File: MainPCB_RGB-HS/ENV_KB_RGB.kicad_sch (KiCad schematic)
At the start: 405 parts

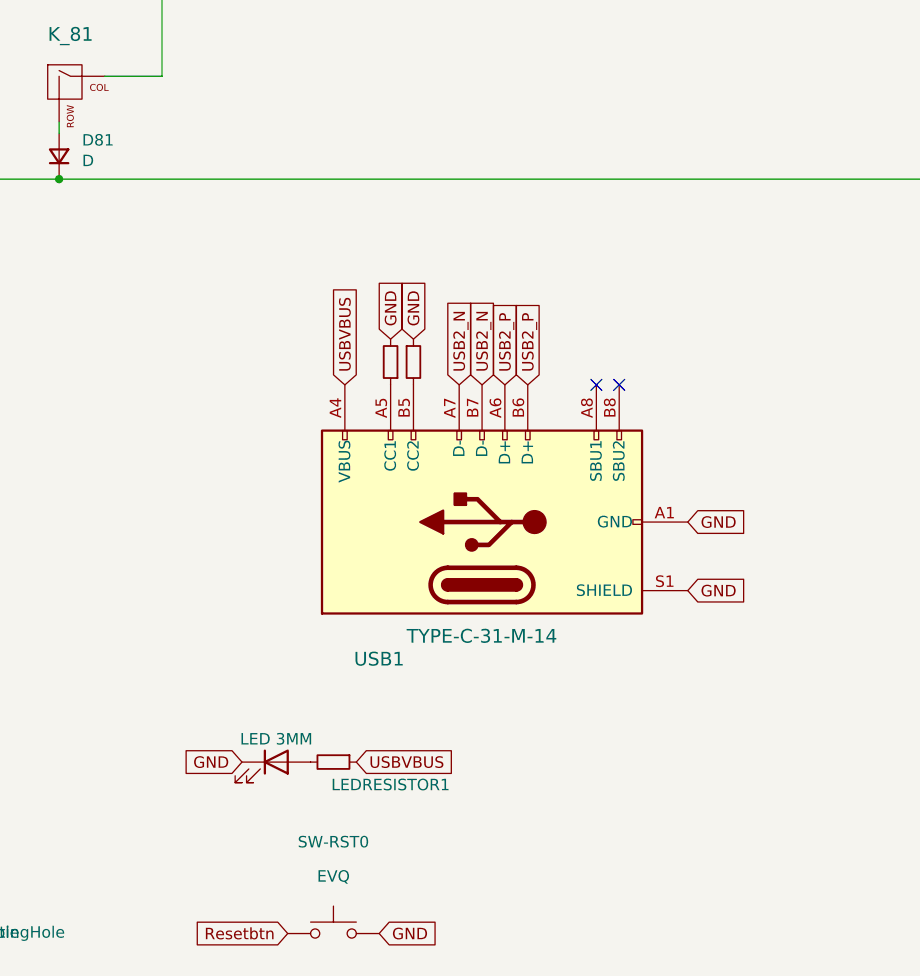
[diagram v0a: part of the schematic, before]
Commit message: added dual footprints and removed experimental version
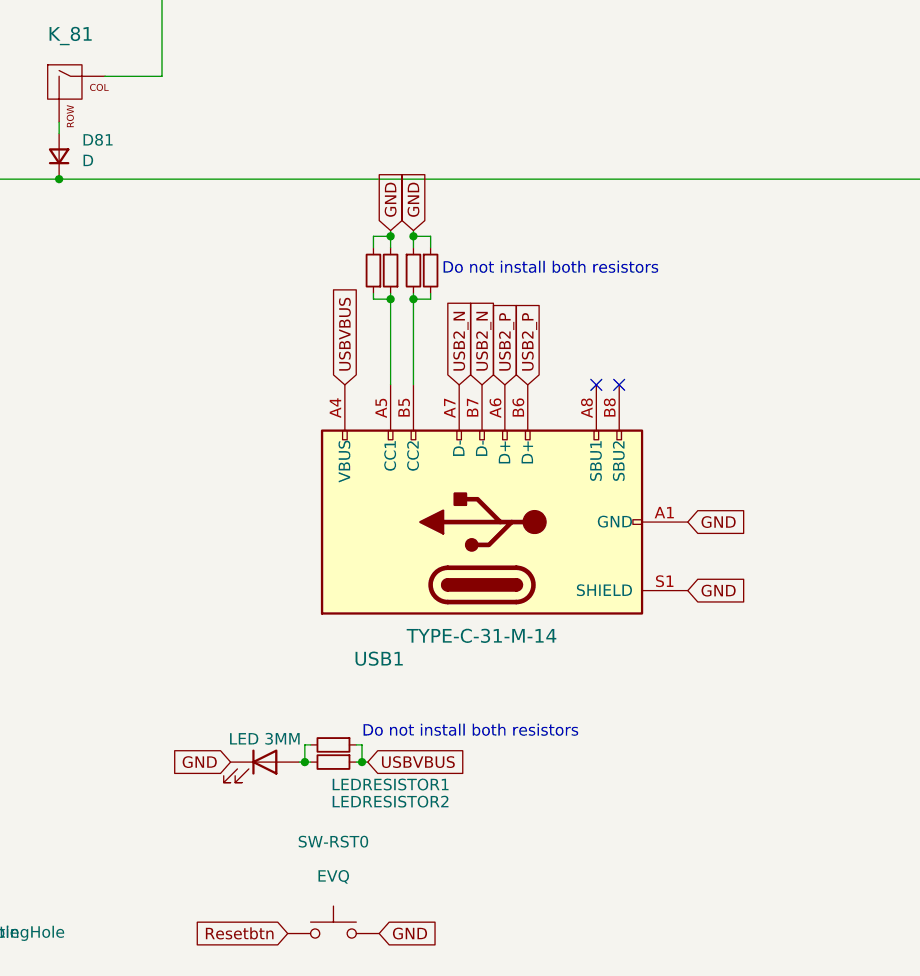
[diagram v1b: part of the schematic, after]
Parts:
- added LEDRESISTOR2: 5.1K Resistor 1/4w, Resistor_SMD:R_0805_2012Metric_Pad1.20x1.40mm_HandSolder, symbol Device:R_Small
- added RESISTOR2, RESISTOR3: 5.1kohm 0805, Resistor_SMD:R_0805_2012Metric, symbol Device:R_Small
- D0, D1, D10, D11, D12, D13, D14, D15, D16, D17, D18, D19, D2, D20, D21, D22, D23, D24, D25, D26, D27, D28, D29, D3, D30, D31, D32, D33, D34, D35, D36, D37, D38, D39, D4, D40, D41, D42, D43, D44, D45, D46, D47, D48, D49, D5, D50, D51, D52, D53, D54, D55, D56, D57, D58, D59, D6, D60, D61, D62, D63, D64, D65, D66, D67, D68, D69, D7, D70, D71, D72, D73, D74, D75, D76, D77, D78, D79, D8, D80, D81, D82, D83, D84, D85, D86, D87, D88, D9: footprint Diode_THT:D_DO-35_SOD27_P7.62mm_Horizontal -> EM_Extras:SOD-123+D_DO-35_SOD27_P7.62mm_Horizontal
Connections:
- net GND: now also RESISTOR2.2, RESISTOR3.1
- net USBVBUS: now also LEDRESISTOR2.1
- net at LEDRESISTOR1.2, PowerLED0.2 (A): now also LEDRESISTOR2.2
- net at RESISTOR1.2, USB1.B5 (CC2): now also RESISTOR3.2
- net at RESISTOR0.1, USB1.A5 (CC1): now also RESISTOR2.1
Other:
- note added: "Do not install both resistors"

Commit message: fixed? ansi+iso+hotswap support I think but also file cleanup
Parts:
- C1, C10, C100, C101, C102, C11, C12, C13, C14, C15, C16, C17, C18, C19, C2, C20, C21, C22, C23, C24, C25, C26, C27, C28, C29, C3, C30, C31, C32, C33, C34, C35, C36, C37, C38, C39, C4, C40, C41, C42, C43, C44, C45, C46, C47, C48, C49, C5, C50, C51, C52, C53, C54, C55, C56, C57, C58, C59, C6, C60, C61, C62, C63, C64, C65, C66, C67, C68, C69, C7, C70, C71, C72, C73, C74, C75, C76, C77, C78, C79, C8, C80, C81, C82, C83, C84, C85, C86, C87, C88, C89, C9, C90, C91, C92, C93, C94, C95, C96, C97, C98, C99: value 100nF 0603 -> (none); footprint Capacitor_SMD:C_0603_1608Metric -> (none)
- D0, D1, D10, D11, D12, D13, D14, D15, D16, D17, D18, D19, D2, D20, D21, D22, D23, D24, D25, D26, D27, D28, D29, D3, D30, D31, D32, D33, D34, D35, D36, D37, D38, D39, D4, D40, D41, D42, D43, D44, D45, D46, D47, D48, D49, D5, D50, D51, D52, D53, D54, D55, D56, D57, D58, D59, D6, D60, D61, D62, D63, D64, D65, D66, D67, D68, D69, D7, D70, D71, D72, D73, D74, D75, D76, D77, D78, D79, D8, D80, D81, D82, D83, D84, D85, D86, D87, D88, D9: value D -> (none); footprint EM_Extras:SOD-123+D_DO-35_SOD27_P7.62mm_Horizontal -> (none)
- H0, H1, H10, H2, H3, H4, H5, H6, H7, H9: value MountingHole -> (none); footprint MountingHole:MountingHole_2.2mm_M2_Pad -> (none)
- K_0, K_1, K_10, K_11, K_12, K_13, K_14, K_15, K_16, K_17, K_18, K_19, K_2, K_20, K_21, K_22, K_23, K_24, K_25, K_26, K_27, K_28, K_29, K_3, K_30, K_31, K_32, K_33, K_34, K_35, K_36, K_37, K_38, K_39, K_4, K_40, K_41, K_42, K_43, K_44, K_45, K_46, K_47, K_48, K_49, K_5, K_50, K_51, K_52, K_53, K_54, K_55, K_56, K_57, K_58, K_59, K_6, K_60, K_61, K_62, K_64, K_64B1, K_65, K_66, K_67, K_68, K_69, K_7, K_70, K_71, K_72, K_73, K_74, K_75, K_76, K_77, K_78, K_79, K_8, K_80, K_81, K_82, K_83, K_84, K_85, K_86, K_87, K_88, K_9: value KEYSW -> (none); footprint MX_Only:MXOnly-1U-Hotswap-Modified -> (none); LCSC (none) -> C2803348
- K_63, K_63B1: value MX-NoLED -> (none); footprint MX_Only:MXOnly-1U-Hotswap-Modified -> (none); LCSC (none) -> C2803348
- LED1, LED10, LED100, LED101, LED102, LED11, LED12, LED13, LED14, LED15, LED16, LED17, LED18, LED19, LED2, LED20, LED21, LED22, LED23, LED24, LED25, LED26, LED27, LED28, LED29, LED3, LED30, LED31, LED32, LED33, LED34, LED35, LED36, LED37, LED38, LED39, LED4, LED40, LED41, LED42, LED43, LED44, LED45, LED46, LED47, LED48, LED49, LED5, LED50, LED51, LED52, LED53, LED54, LED55, LED56, LED57, LED58, LED59, LED6, LED60, LED61, LED62, LED63, LED64, LED65, LED66, LED67, LED68, LED69, LED7, LED70, LED71, LED72, LED73, LED74, LED75, LED76, LED77, LED78, LED79, LED8, LED80, LED81, LED82, LED83, LED84, LED85, LED86, LED87, LED88, LED89, LED9, LED90, LED91, LED92, LED93, LED94, LED95, LED96, LED97, LED98, LED99: value SK6812MINI-E -> (none); footprint sk6812mini:MX_SK6812MINI-E_REV -> (none)
- LEDRESISTOR1: value 5.1K Resistor 1/4w -> (none); footprint Resistor_THT:R_Axial_DIN0207_L6.3mm_D2.5mm_P10.16mm_Horizontal -> (none)
- LEDRESISTOR2: value 5.1K Resistor 1/4w -> (none); footprint Resistor_SMD:R_0805_2012Metric_Pad1.20x1.40mm_HandSolder -> (none)
- PowerLED0: value LED 3MM -> (none); footprint LED_THT:LED_D3.0mm_FlatTop -> (none)
- RESISTOR0: value 5.1kohm 1/4w -> (none); footprint Resistor_THT:R_Axial_DIN0207_L6.3mm_D2.5mm_P10.16mm_Horizontal -> (none)
- RESISTOR1: value 5.1kohm 1/4 -> (none); footprint Resistor_THT:R_Axial_DIN0207_L6.3mm_D2.5mm_P10.16mm_Horizontal -> (none)
- RESISTOR2, RESISTOR3: value 5.1kohm 0805 -> (none); footprint Resistor_SMD:R_0805_2012Metric -> (none)
- RPI0: value Pico -> (none); footprint EM_Extras:RPi_Pico_SMD_TH -> (none)
- SW-RST0: value EVQ -> (none); footprint Button_Switch_SMD:Panasonic_EVQPUM_EVQPUD -> (none)
- Stab1: value Stabilizer -> (none); footprint Mounting_Keyboard_Stabilizer:Stabilizer_Cherry_MX_6.25u -> (none)
- Stab2, Stab3, Stab4: value Stabilizer -> (none); footprint Mounting_Keyboard_Stabilizer:Stabilizer_Cherry_MX_2u -> (none)
- USB1: value TYPE-C-31-M-14 -> (none); footprint josh-connectors:USB_C_TYPE-C-31-M-14 -> (none)
